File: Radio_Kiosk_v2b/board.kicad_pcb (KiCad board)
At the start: 2 copper layers, 84 x 133 mm, 228 parts, among them J1 USB-C PD in, J11 UART, J12 USB-C, J13 Lid LEDs, J2 DC in 18-26V, PJ-002BH 5.5x2.5, J3 Laptop out 15.6V, PJ-002BH 5.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, J5 RJ45 radio, J6 RJ45 laptop, J8 Fan 12V, J9 SWD, Q1 SI4470EY, Q10 2N7002, Q11 AO3400A, Q12 SI4470EY, Q13 AO4482, Q2 SI4470EY, Q20 AO4482, Q22 PSMN075-100MSEX, Q23 DMP10H400SE, Q24 BSS123, Q25 2N7002, Q30 AO3400A, Q40 AOD4184A, Q41 AOD4184A, Q6 SI4470EY, Q7 SI4470EY, Q8 AOD4185, Q9 2N7002, SW1 RESET, SW2 BOOT0 (DFU), U1 LM74700-Q1, U10 TLV7011, U12 LM74700-Q1, U2 LM74700-Q1, U20 LM3478 54V boost, U21 TPS26600 eFuse, U22 LTC4279, U3 LMR33630 12V, U30 SN74AHCT1G125, U31 SN74AHCT1G125, U4 LM3150 15.75V 4.5A, U40 STM32F072CBT6, U41 INA180A1, U42 INA180A1, U43 MCP6001T-I/OT, U5 LMR33630 5V, U50 CH224A, U51 AP2112K-3.3, U52 USBLC6-2SC6, U6 LM74700-Q1, U7 LM74700-Q1

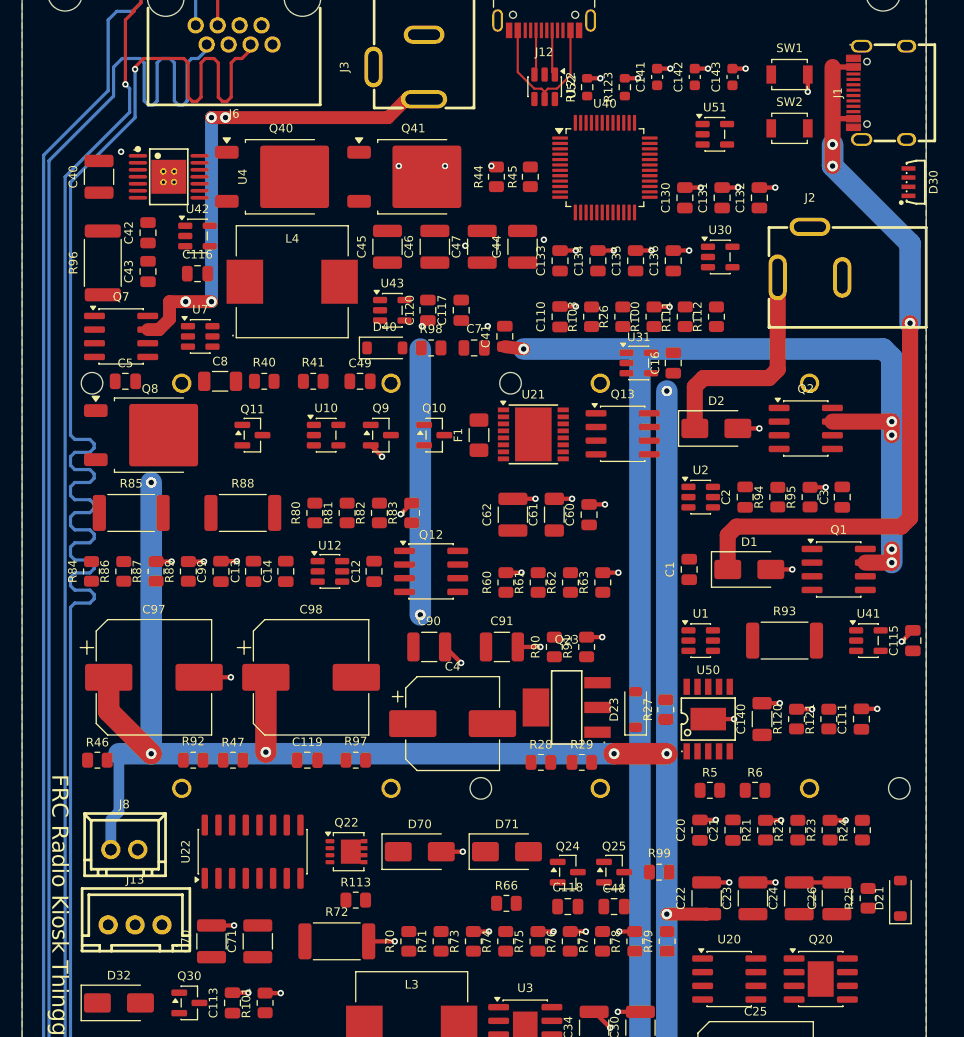
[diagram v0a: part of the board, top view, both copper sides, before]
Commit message: v2b: second audit fixes
Laptop rail: RON 820k (~190 kHz, clears the 725 ns minimum off-time at 20 V),
L4 15 uH, output bank 22u ceramic + 220u/25V polymer (ESR window), CFF 2.2n,
RLIM 750R, LAPTOP_OK divider to PC13 for a shorted jack. Port: eFuse ILIM
5.6k (in the 5.36k-120k range), dV/dt 47n, boost FB 499k (53.7 V, inside the
LTC4279 window over tolerance), 100k bleeder on BOOST_OUT. Comments fixed.

Co-Authored-By: Claude Fable 5.1 <noreply@anthropic.com>
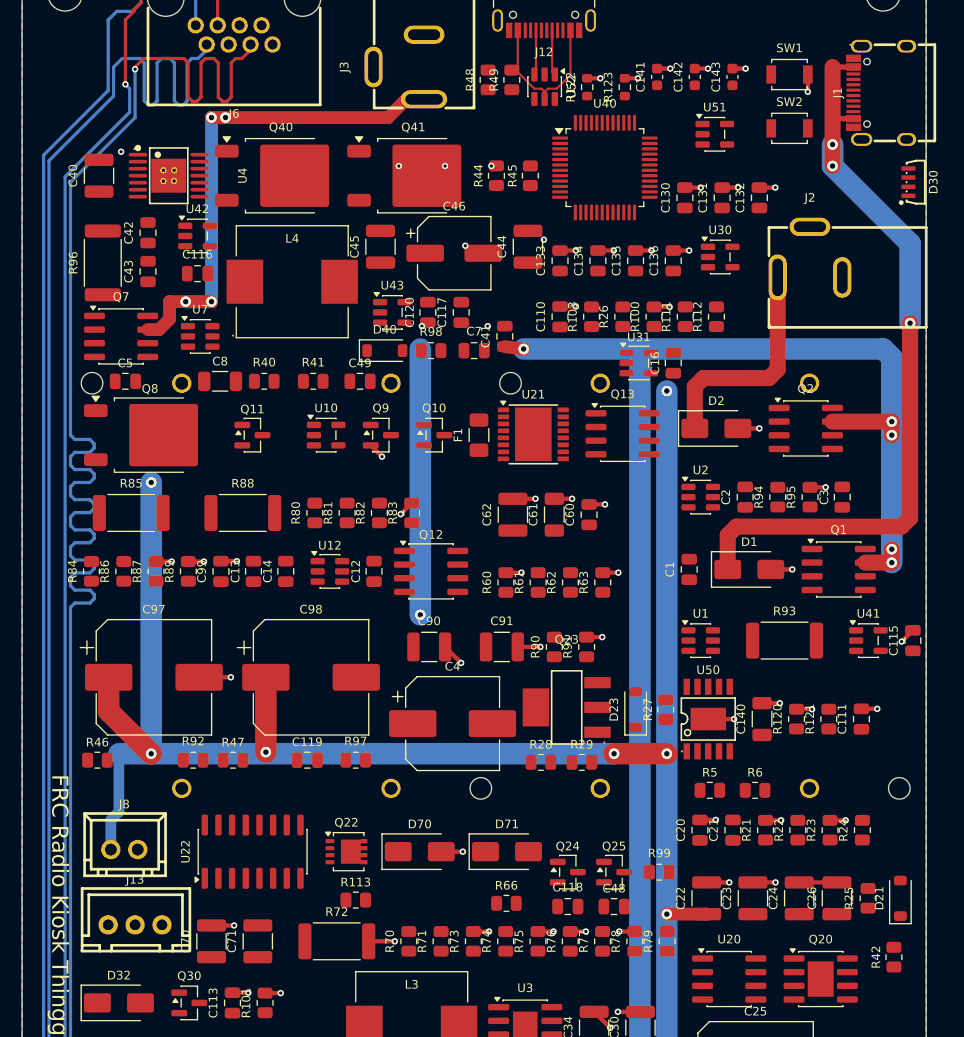
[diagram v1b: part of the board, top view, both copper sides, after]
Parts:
- removed C47: 22u/25V, Capacitor_SMD:C_1210_3225Metric
- added R42: 100k, R_0805_2012Metric, F.Cu at (81.0, 93.5)
- added R48: 47k, R_0805_2012Metric, F.Cu at (43.3, 12.0)
- added R49: 10k, R_0805_2012Metric, F.Cu at (45.5, 12.0)
- C46: value 22u/25V -> 220u/25V polymer; footprint Capacitor_SMD:C_1210_3225Metric -> CP_Elec_6.3x7.7
- C49: value 220p -> 2.2n
- C60: value 10n -> 47n
- L20: value MDA1365-330M 33u 4.5A -> MDA1365-330M 33u 9A
- L4: value MDA1040-100M 10u 8A -> MDA1040-150M 15u 6A
- R22: value 510k -> 499k 1%
- R44: value 510k -> 820k
- R45: value 680R -> 750R
- R60: value 5.1k -> 5.6k
- moved C46 1.90 mm to (40.1, 28.1), turned to 0 degrees
- moved C45 0.65 mm to (33.3, 27.5)
- moved C44 0.50 mm to (47.0, 27.5)
- moved C7 0.25 mm to (42.0, 37.1)
- moved D40 0.25 mm to (33.7, 37.1)
- moved R98 0.25 mm to (38.0, 37.1)
- moved C117 0.20 mm to (40.8, 33.6)
- moved C120 0.20 mm to (37.7, 33.6)
- moved U43 0.20 mm to (34.4, 33.6)
- moved C40 0.10 mm to (7.15, 20.9)
- moved Q40 0.10 mm to (24.1, 20.9)
- moved Q41 0.10 mm to (36.4, 20.9)
- moved R44 0.10 mm to (44.1, 20.9)
- moved R45 0.10 mm to (47.2, 20.9)
- moved U4 0.10 mm to (13.6, 20.9)
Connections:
- U40 pad 2: (no net) -> LAPTOP_OK

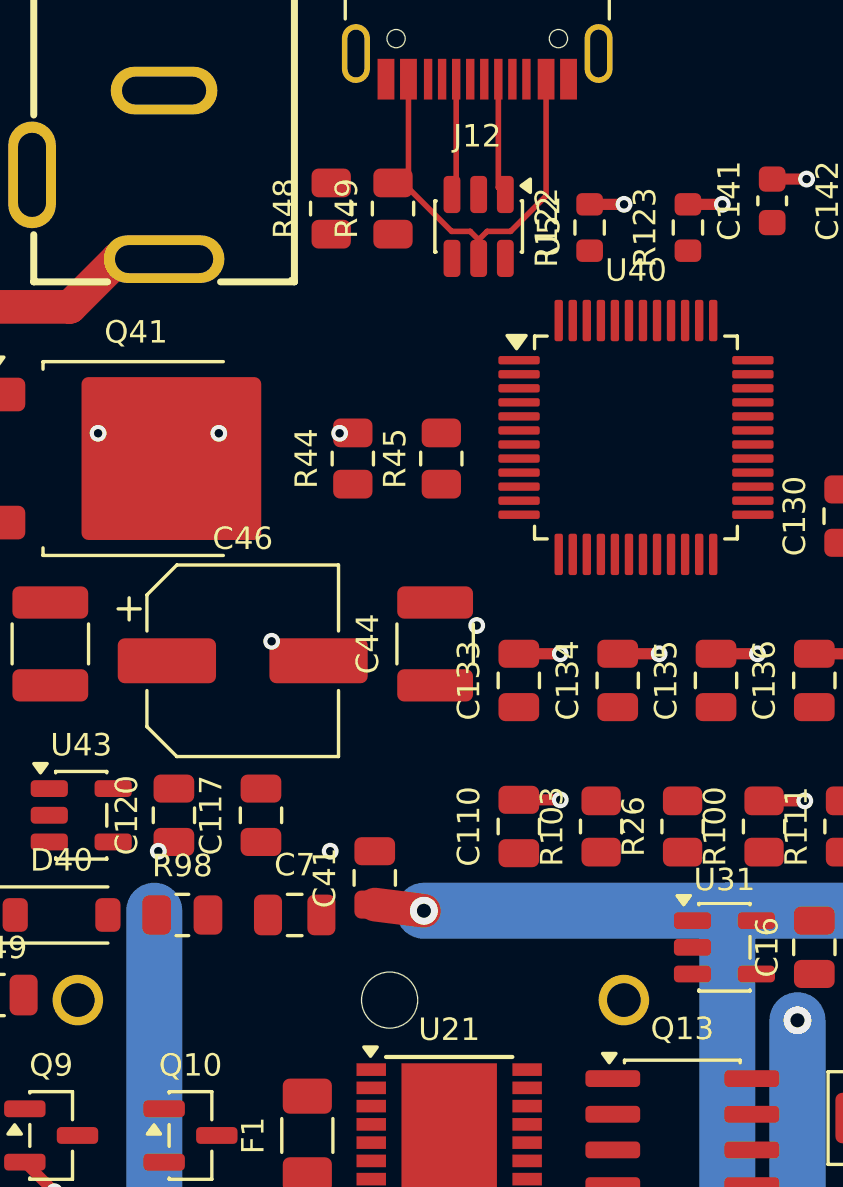
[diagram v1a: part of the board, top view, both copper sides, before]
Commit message: v2b: jack-sense divider moved off the VBUS trace
Co-Authored-By: Claude Fable 5.1 <noreply@anthropic.com>
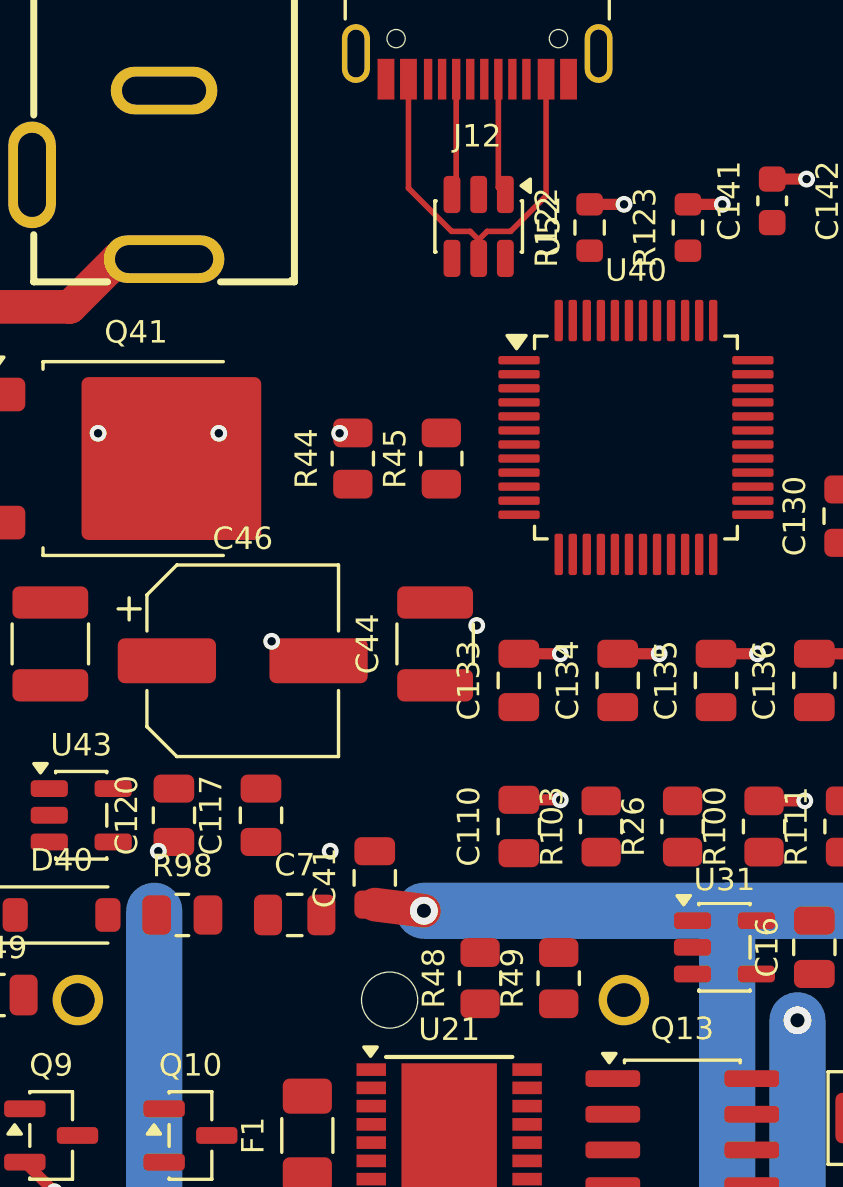
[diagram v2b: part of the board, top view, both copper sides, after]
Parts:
- moved R49 28.0 mm to (51.4, 39.4)
- moved R48 27.9 mm to (48.6, 39.4)
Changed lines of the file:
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@@
 	(footprint "R_0805_2012Metric"
 		(layer "F.Cu")
-		(at 43.3 12 90)
+		(at 48.6 39.4 90)
 		(descr "Resistor SMD 0805 (2012 Metric), square (rectangular) end terminal, IPC-7351 nominal, (Body size source: IPC-SM-782 page 72, https://www.pcb-3d.com/wordpress/wp-content/uploads/ipc-sm-782a_amendment_1_and_2.pdf)")
 		(tags "resistor")
@@
 	(footprint "R_0805_2012Metric"
 		(layer "F.Cu")
-		(at 45.5 12 90)
+		(at 51.4 39.4 90)
 		(descr "Resistor SMD 0805 (2012 Metric), square (rectangular) end terminal, IPC-7351 nominal, (Body size source: IPC-SM-782 page 72, https://www.pcb-3d.com/wordpress/wp-content/uploads/ipc-sm-782a_amendment_1_and_2.pdf)")
 		(tags "resistor")

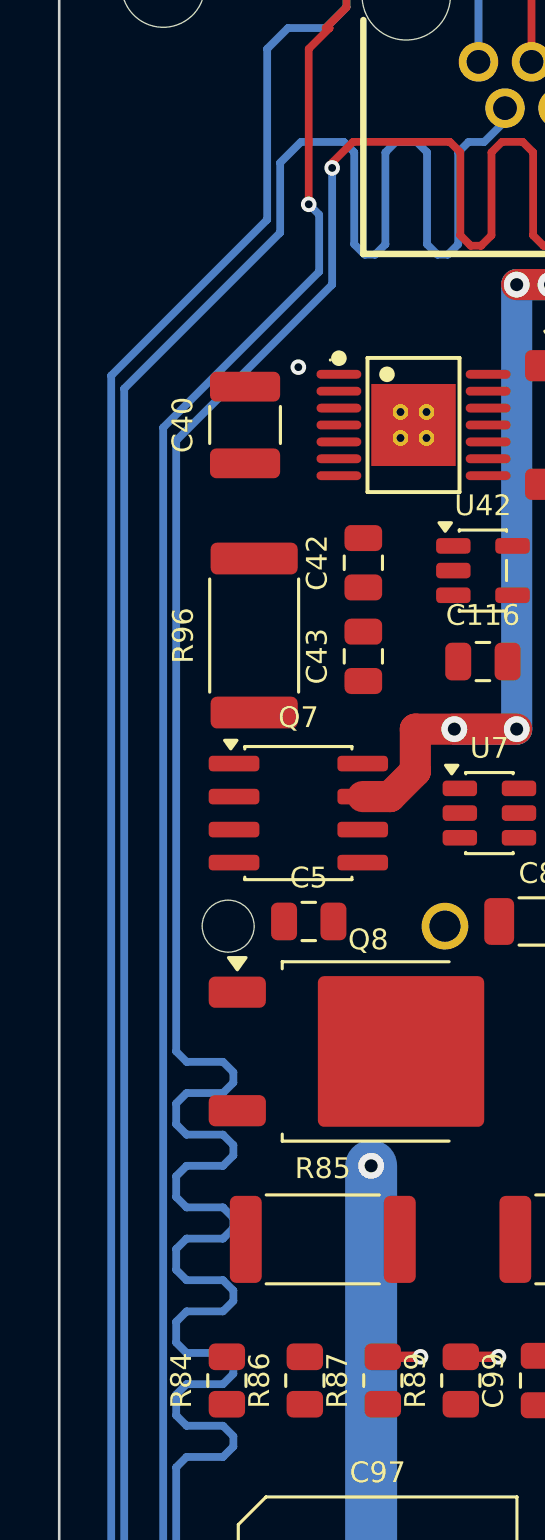
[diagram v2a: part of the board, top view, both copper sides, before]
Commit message: v2b: interlocked laptop bypass for a 16 V brick
Q44 SI4401DDY from VIN to +15V6_S (source on VIN, body diode blocks), gate
through 10k/47k from Q45, BZT52C12 clamp. U45 TLV7011 compares VIN_SENSE with
a 2.2 V reference that only exists while PC14 LAPTOP_BYP is high, so the
bypass closes only below ~17.6 V and only on firmware's say-so. Parts along
the left edge by the laptop rail; front side only. tools: text-based clone
and placer; the pcbnew swap path dropped 44 footprints once and is retired.

Co-Authored-By: Claude Fable 5.1 <noreply@anthropic.com>
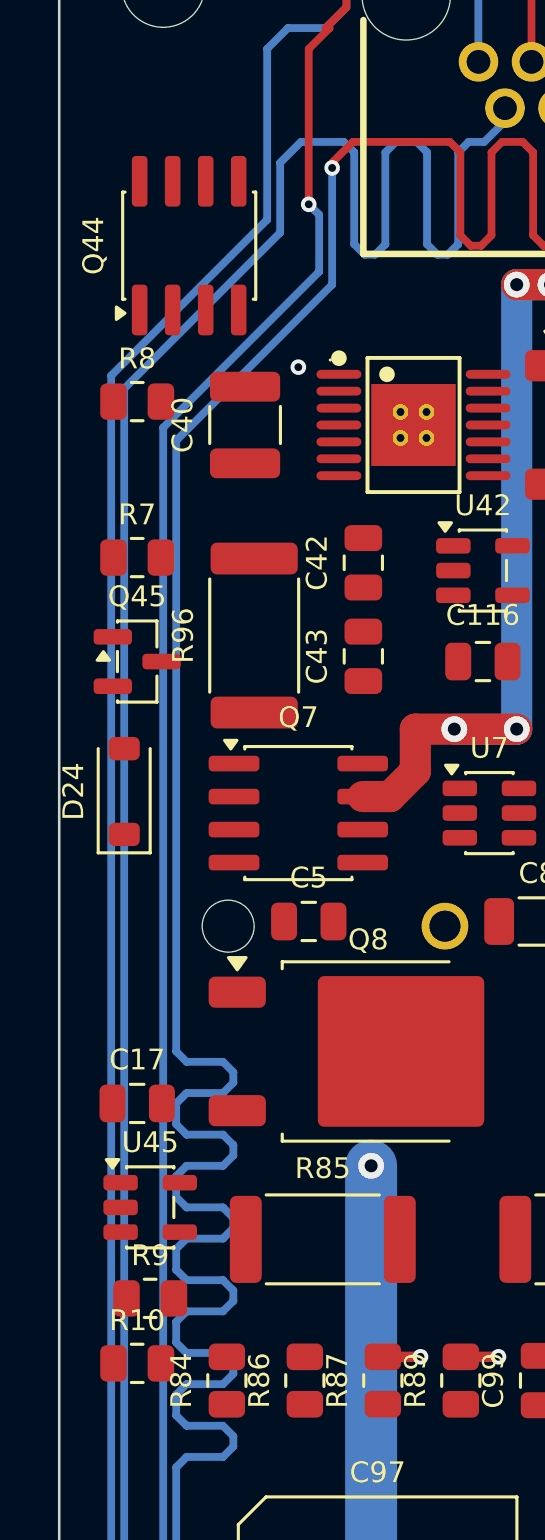
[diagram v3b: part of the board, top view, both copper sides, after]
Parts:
- added C17: 100n, C_0805_2012Metric, F.Cu at (3.00, 47.0)
- added D24: BZT52C12 zener, Diode_SMD:D_SOD-123, F.Cu at (2.50, 35.0)
- added Q44: SI4401DDY, Package_SO:SOIC-8_3.9x4.9mm_P1.27mm, F.Cu at (5.00, 14.0)
- added Q45: 2N7002, Package_TO_SOT_SMD:SOT-23, F.Cu at (3.00, 30.0)
- added R10: 20k, R_0805_2012Metric, F.Cu at (3.00, 57.0)
- added R7: 10k, R_0805_2012Metric, F.Cu at (3.00, 26.0)
- added R8: 47k, R_0805_2012Metric, F.Cu at (3.00, 20.0)
- added R9: 10k, R_0805_2012Metric, F.Cu at (3.50, 54.5)
- added U45: TLV7011, Package_TO_SOT_SMD:SOT-23-5, F.Cu at (3.50, 51.0)

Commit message: v2b: board restored after loon's save overwrote it; VIN_DC 2 mm, second via on the VIN_USB corner
Co-Authored-By: Claude Fable 5.1 <noreply@anthropic.com>
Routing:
- net VIN_USB: track 71.5 -> 72.9 mm, vias 3 -> 4
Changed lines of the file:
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@@
 		(start 70.2 38.9)
 		(end 69.4 39.7)
-		(width 1.5)
+		(width 2)
 		(layer "F.Cu")
 		(net "VIN_DC")
@@
 		(start 63.3 39.7)
 		(end 62.5 40.5)
-		(width 1.5)
+		(width 2)
 		(layer "F.Cu")
 		(net "VIN_DC")
@@
 		(start 69.4 39.7)
 		(end 63.3 39.7)
-		(width 1.5)
+		(width 2)
 		(layer "F.Cu")
 		(net "VIN_DC")
@@
 		(start 62.5 40.5)
 		(end 62.5 44.38)
-		(width 1.5)
+		(width 2)
 		(layer "F.Cu")
 		(net "VIN_DC")
@@
 		(start 70.2 30.35)
 		(end 70.2 38.9)
-		(width 1.5)
+		(width 2)
 		(layer "F.Cu")
 		(net "VIN_DC")
@@
 		(net "BK_ARM")
 	)
+	(segment
+		(start 82.5 34.6)
+		(end 82.5 36)
+		(width 2)
+		(layer "B.Cu")
+		(net "VIN_USB")
+	)
+	(via
+		(at 82.5 36)
+		(size 1)
+		(drill 0.5)
+		(layers "F.Cu" "B.Cu")
+		(net "VIN_USB")
+	)
 	(zone

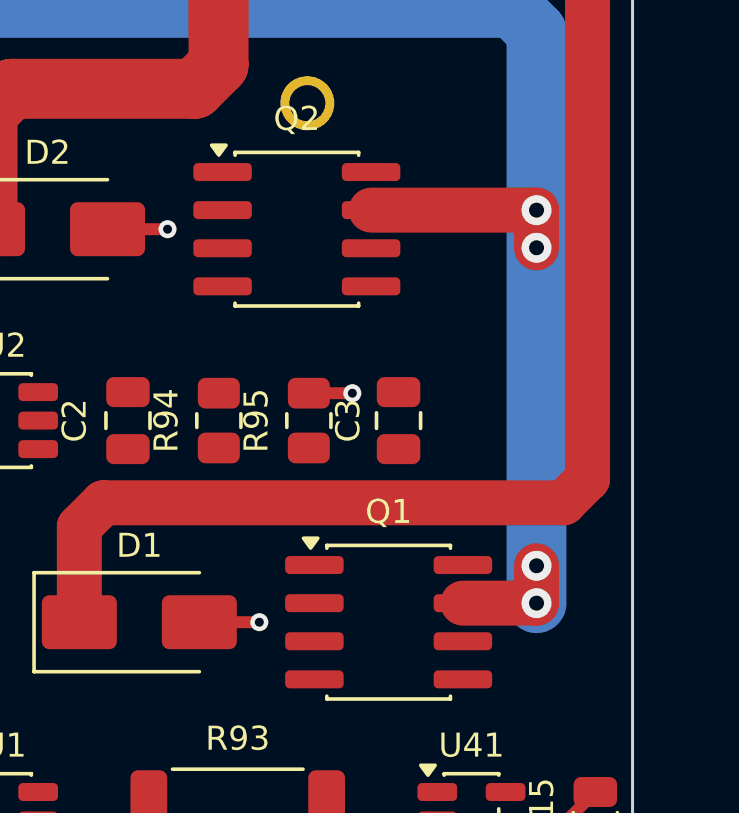
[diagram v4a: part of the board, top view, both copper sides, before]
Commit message: v2b: 2 mm stubs from the input FET drains to the VIN spine
Co-Authored-By: Claude Fable 5.1 <noreply@anthropic.com>
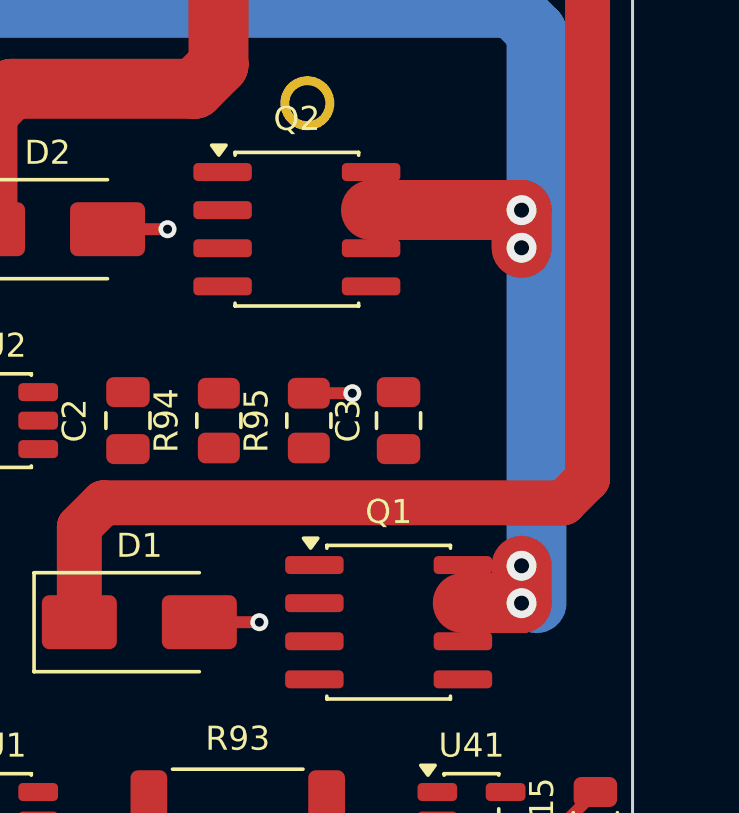
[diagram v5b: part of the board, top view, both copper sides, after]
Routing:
- net VIN: track 130.3 -> 129.4 mm
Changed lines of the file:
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@@
 	)
 	(segment
-		(start 75.285 43.745)
-		(end 80.8 43.745)
-		(width 1.5)
+		(start 75.28 43.74)
+		(end 80.3 43.74)
+		(width 2)
 		(layer "F.Cu")
 		(net "VIN")
 	)
 	(segment
-		(start 80.8 56.84)
-		(end 80.8 55.6)
-		(width 1.5)
+		(start 80.3 56.84)
+		(end 80.3 55.6)
+		(width 2)
 		(layer "F.Cu")
 		(net "VIN")
 	)
 	(segment
-		(start 80.8 43.74)
-		(end 80.8 45)
-		(width 1.5)
+		(start 80.3 43.74)
+		(end 80.3 45)
+		(width 2)
 		(layer "F.Cu")
 		(net "VIN")
 	)
 	(segment
-		(start 78.345 56.845)
-		(end 80.8 56.845)
-		(width 1.5)
+		(start 78.34 56.84)
+		(end 80.3 56.84)
+		(width 2)
 		(layer "F.Cu")
 		(net "VIN")
@@
 	)
 	(via
-		(at 80.8 56.845)
+		(at 80.3 56.845)
 		(size 1)
 		(drill 0.5)
@@
 	)
 	(via
-		(at 80.8 55.6)
+		(at 80.3 55.6)
 		(size 1)
 		(drill 0.5)
@@
 	)
 	(via
-		(at 80.8 43.745)
+		(at 80.3 43.745)
 		(size 1)
 		(drill 0.5)
@@
 	)
 	(via
-		(at 80.8 45)
+		(at 80.3 45)
 		(size 1)
 		(drill 0.5)
